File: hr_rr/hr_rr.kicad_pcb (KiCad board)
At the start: 2 copper layers, 32.2 x 20.5 mm, 44 parts, among them P1 Conn_01x02_Male, P2 Conn_01x02_Male, P3 Conn_01x02_Male, Q1 DMP21D5UFB4-7B, U1 TPS62746, U2 TPS63051_YFF, U3 NRF528XX-QFAA, U6 MCP73831, X1 Crystal_GND24, X2 32.768 kHz

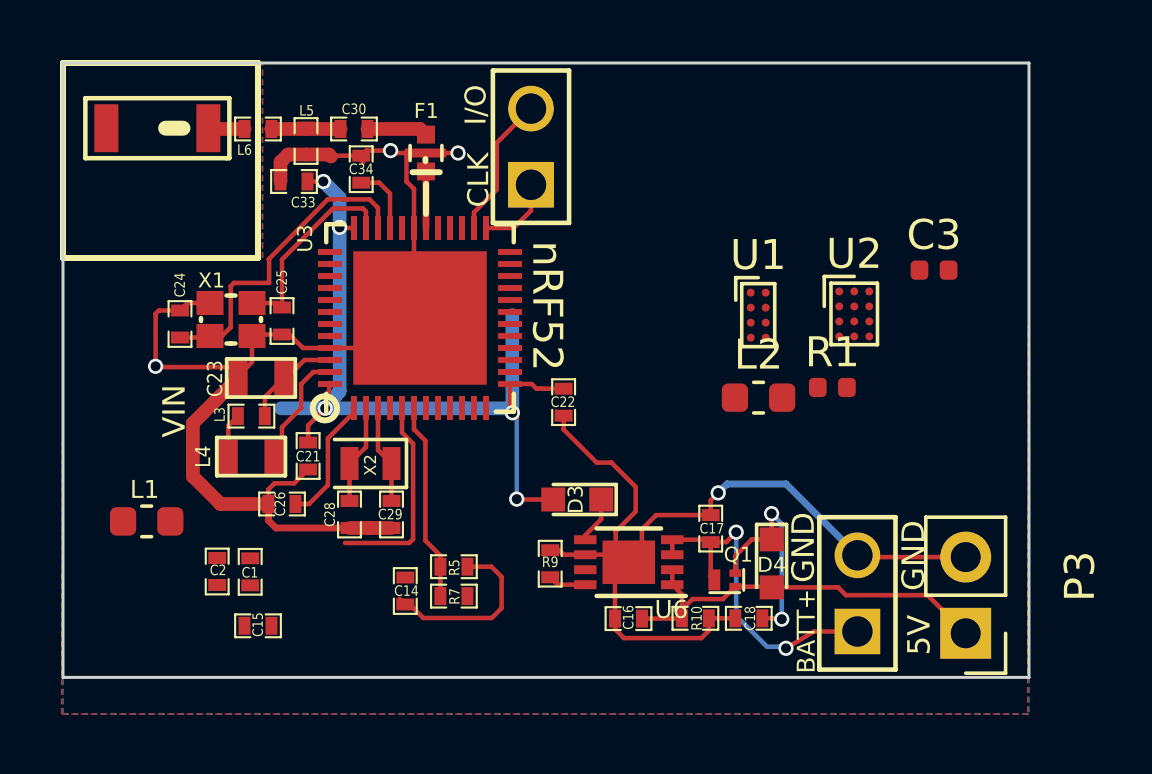
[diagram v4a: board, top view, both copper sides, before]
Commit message: Changed TPS63051 to VQFN Version, integrated power components.
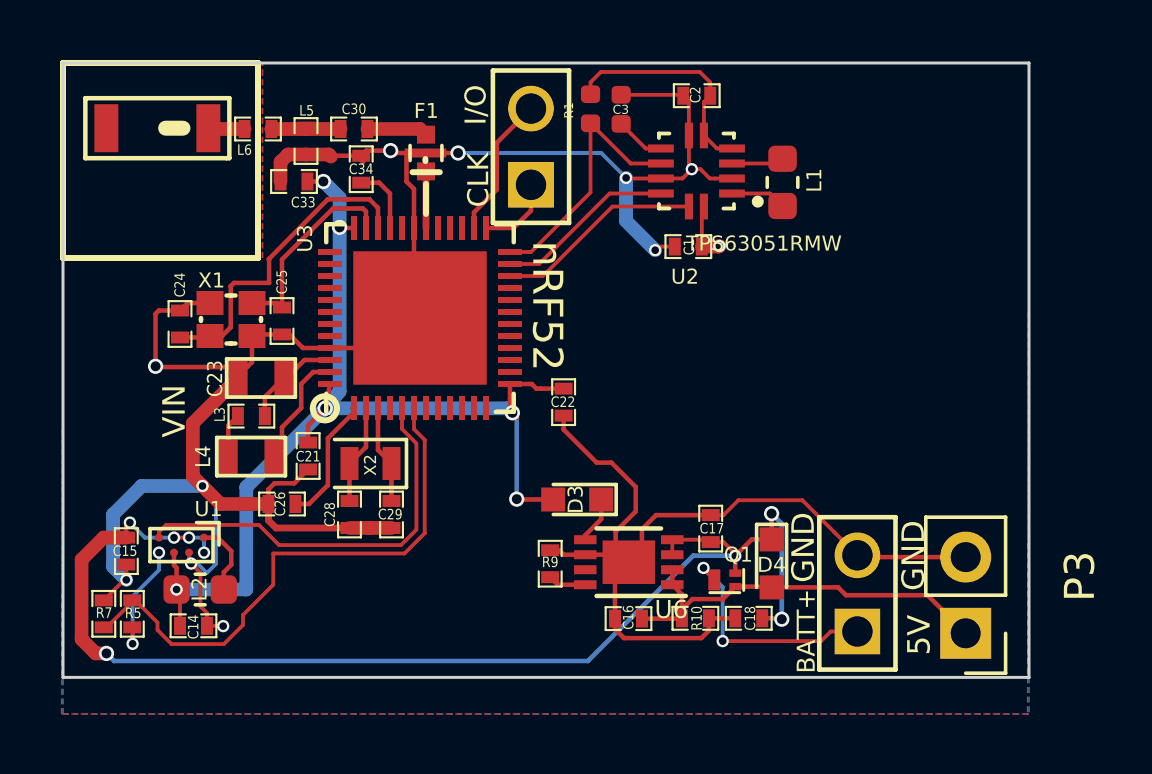
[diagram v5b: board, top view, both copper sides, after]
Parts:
- U2: value TPS63051_YFF -> TPS63051RMW; footprint Package_BGA:Texas_DSBGA-12_1.36x1.86mm_Layout3x4_P0.5mm -> footprints:QFN50P250X250X100-12N
- moved L1 24.0 mm to (289.9, 129.5), turned to 270 degrees
- moved C2 22.5 mm to (287.0, 126.6), turned to 180 degrees
- moved U1 20.7 mm to (269.9, 141.6), turned to 270 degrees
- moved L2 19.7 mm to (270.5, 143.1), turned to 180 degrees
- moved C1 18.2 mm to (286.7, 131.6), turned to 180 degrees
- moved R1 12.3 mm to (283.5, 127.0), turned to 270 degrees
- moved C3 11.7 mm to (284.5, 127.0), turned to 90 degrees
- moved R7 11.7 mm to (267.3, 143.9), turned to 270 degrees
- moved R5 10.8 mm to (268.2, 143.9), turned to 90 degrees
- moved C14 7.15 mm to (270.2, 144.3), turned to 0 degrees
- moved U2 7.10 mm to (287.0, 129.1), turned to 180 degrees
- moved C15 5.05 mm to (268.0, 141.8), turned to 270 degrees
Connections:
- C17 pad 1: /BATT_IN -> Vcc<BATT>
- U3 pad 22: Net-(U3-Pad22) -> /EN_TPS63051
- U3 pad 23: Net-(U3-Pad23) -> /ILIM0_TPS63051
- U3 pad 24: Net-(U3-Pad24) -> /PG_TPS63051
- U3 pad 7: /PG_TPS63051 -> Net-(U3-Pad7)
- U3 pad 8: /ILIM0_TPS63051 -> Net-(U3-Pad8)
- U3 pad 9: /ILIM1_TPS63051 -> Net-(U3-Pad9)
- U6 pad 3: /BATT_IN -> Vcc<BATT>
- U6 pad 4: /BATT_IN -> Vcc<BATT>
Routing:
- net Vcc<BATT>: track 7.20 -> 43.7 mm, vias 2 -> 9
- net DGND: track 85.0 -> 116.5 mm, vias 4 -> 10
- net /AIN_BAT_DIV_VOLTAGE: track 6.63 -> 18.5 mm
- net /BATT_IN: track 11.5 -> 0.00 mm, vias 2 -> 0
- net /PG_TPS63051: track 0.00 -> 8.96 mm
- net BATT_V: track 0.00 -> 8.05 mm, vias 0 -> 2
- net 3.3V_supply: track 0.00 -> 7.64 mm
- net 1.8V_supply: track 29.6 -> 36.9 mm, vias 5 -> 6
- net /EN_TPS63051: track 0.00 -> 6.92 mm
- net /LOAD_SW_CTRL: track 6.85 -> 13.6 mm
- net Net-(C14-Pad1): track 6.12 -> 0.00 mm
- net /ILIM0_TPS63051: track 0.00 -> 6.00 mm
- net Net-(R5-Pad1): track 0.00 -> 3.96 mm, vias 0 -> 2
- net Net-(L2-Pad1): track 0.00 -> 2.48 mm
- net Net-(L1-Pad2): track 0.00 -> 1.86 mm
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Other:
- net class Default: clearance 0.1524 -> 0.127; trace_width 0.4572 -> 0.127
- rule trace_clearance: 0.1524 -> 0.127
- rule via_min_drill: 0.3302 -> 0.254
- rule via_min_size: 0.152 -> 0.127

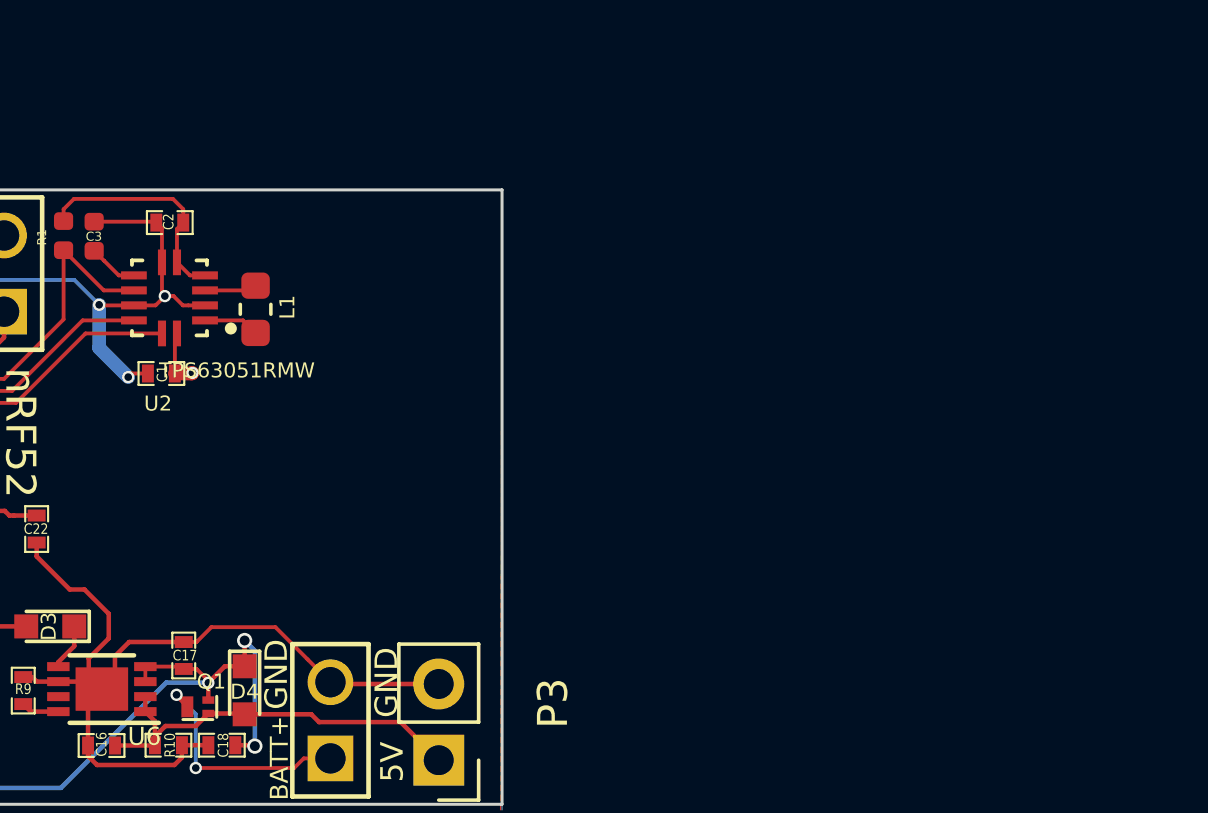
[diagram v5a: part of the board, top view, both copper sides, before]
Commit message: Added footprint for CMOS clock, added to PCB.
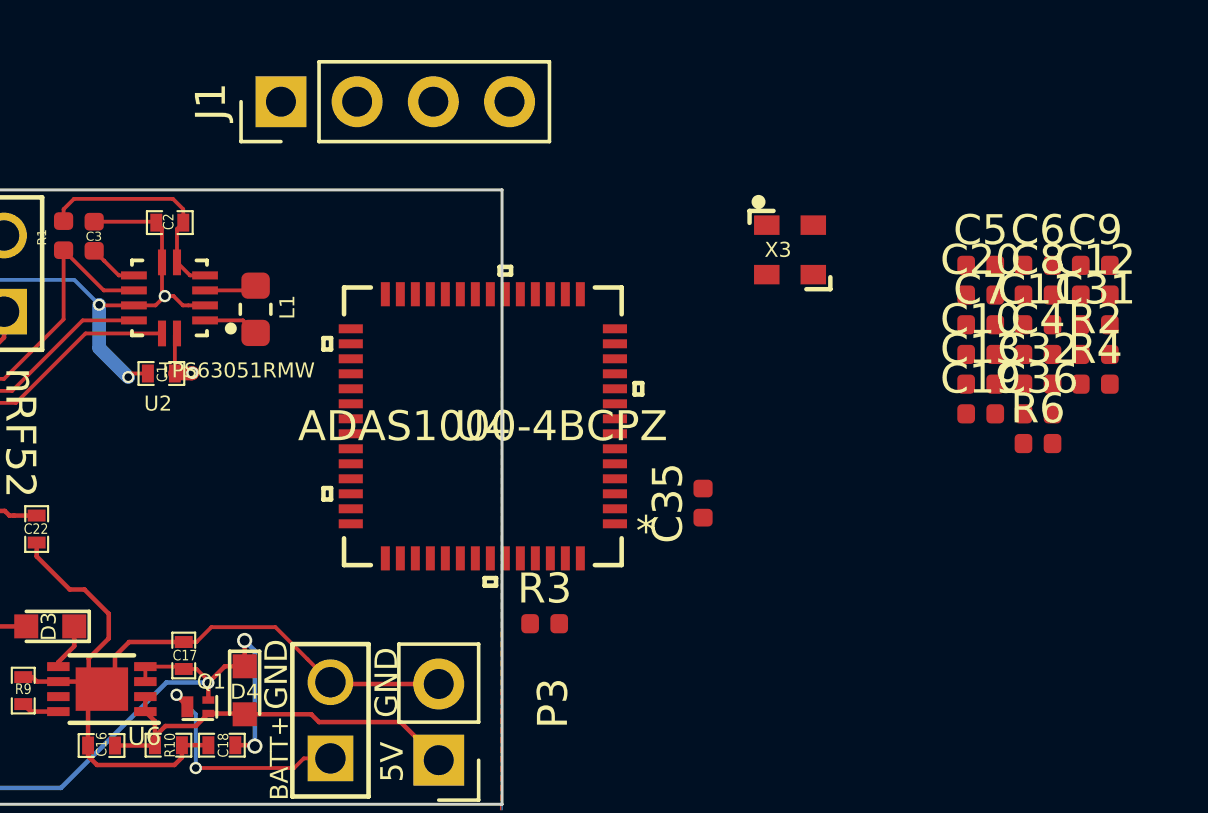
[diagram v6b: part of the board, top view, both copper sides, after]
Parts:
- added C10: 0.1uF, Capacitor_SMD:C_0402_1005Metric, F.Cu at (314.1, 131.0)
- added C11: 0.1uF, Capacitor_SMD:C_0402_1005Metric, F.Cu at (316.0, 130.0)
- added C12: 0.1uF, Capacitor_SMD:C_0402_1005Metric, F.Cu at (317.9, 129.0)
- added C13: 0.1uF, Capacitor_SMD:C_0402_1005Metric, F.Cu at (314.1, 132.0)
- added C19: 0.1uF, Capacitor_SMD:C_0402_1005Metric, F.Cu at (314.1, 133.0)
- added C20: 0.1uF, Capacitor_SMD:C_0402_1005Metric, F.Cu at (314.1, 129.0)
- added C31: 2.2 nF, Capacitor_SMD:C_0402_1005Metric, F.Cu at (317.9, 130.0)
- added C32: 0.1uF, Capacitor_SMD:C_0402_1005Metric, F.Cu at (316.0, 132.0)
- added C35: 10uF, Capacitor_SMD:C_0402_1005Metric, F.Cu at (304.8, 135.9)
- added C36: 15pF, Capacitor_SMD:C_0402_1005Metric, F.Cu at (316.0, 133.0)
- added C4: 4.7uF, Capacitor_SMD:C_0402_1005Metric, F.Cu at (316.0, 131.0)
- added C5: 4.7uF, Capacitor_SMD:C_0402_1005Metric, F.Cu at (314.1, 128.0)
- added C6: 0.1uF, Capacitor_SMD:C_0402_1005Metric, F.Cu at (316.0, 128.0)
- added C7: 0.1uF, Capacitor_SMD:C_0402_1005Metric, F.Cu at (314.1, 130.0)
- added C8: 0.1uF, Capacitor_SMD:C_0402_1005Metric, F.Cu at (316.0, 129.0)
- added C9: 0.1uF, Capacitor_SMD:C_0402_1005Metric, F.Cu at (317.9, 128.0)
- added J1: Electrodes, Connector_PinHeader_2.54mm:PinHeader_1x04_P2.54mm_Vertical, F.Cu at (290.7, 122.6)
- added R2: 4M, Resistor_SMD:R_0402_1005Metric, F.Cu at (317.9, 131.0)
- added R3: 40k, Resistor_SMD:R_0402_1005Metric, F.Cu at (299.5, 140.0)
- added R4: 100k, Resistor_SMD:R_0402_1005Metric, F.Cu at (317.9, 132.0)
- added R6: 30k, Resistor_SMD:R_0402_1005Metric, F.Cu at (316.0, 134.0)
- added U4: ADAS1000-4BCPZ, footprints:ADAS1000-4BCPZ, F.Cu at (297.5, 133.4)
- added X3: DSC1001, footprints:DSC1001DI5-008.1920T, F.Cu at (307.7, 127.5)
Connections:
- U3 pad 14: Net-(U3-Pad14) -> /~CS
- U3 pad 15: Net-(U3-Pad15) -> /~DRDY
- U3 pad 16: Net-(U3-Pad16) -> /SDI
- U3 pad 17: Net-(U3-Pad17) -> /SCLK
- U3 pad 18: Net-(U3-Pad18) -> /SDO
- U3 pad 19: Net-(U3-Pad19) -> /~PWDN
- U3 pad 20: Net-(U3-Pad20) -> /~RESET
- U3 pad 21: Net-(U3-Pad21) -> /CLK_DSC1001_STANDBY

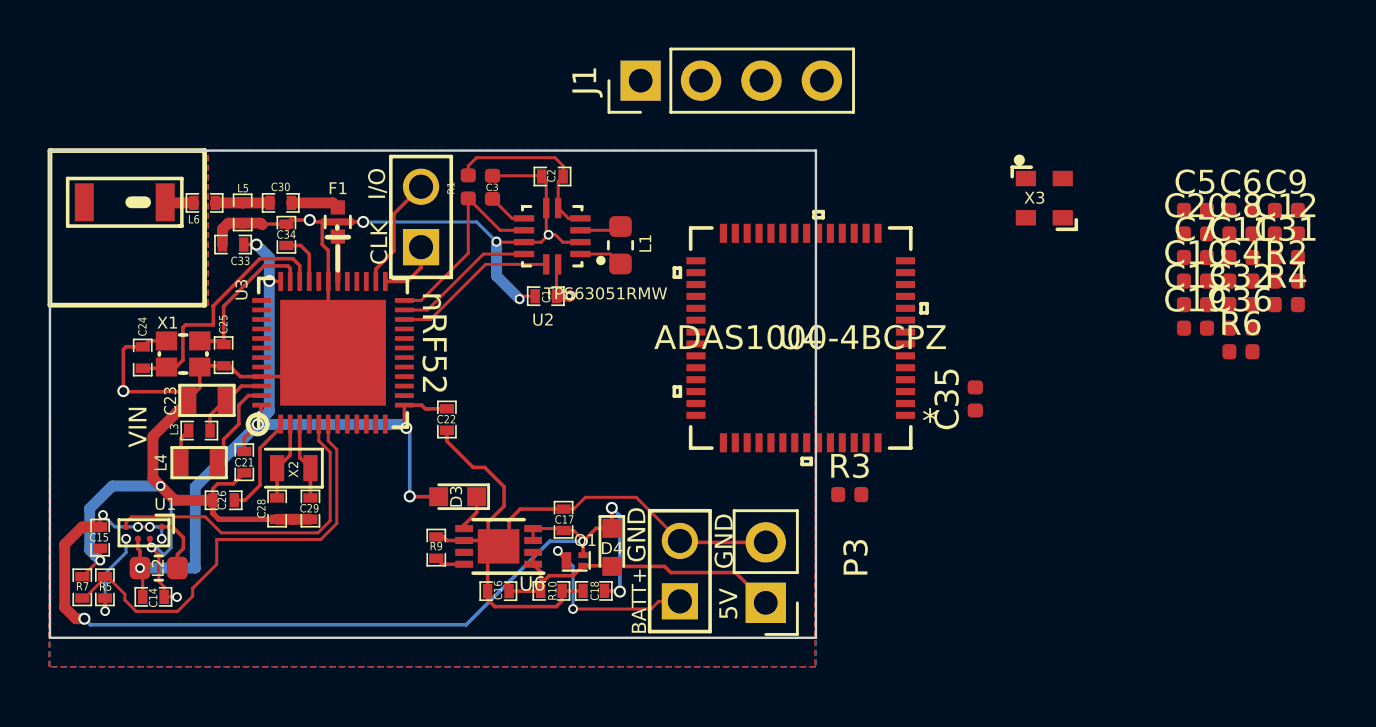
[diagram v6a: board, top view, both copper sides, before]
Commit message: Completed ADAS1000-4 portion, finalized PCB.
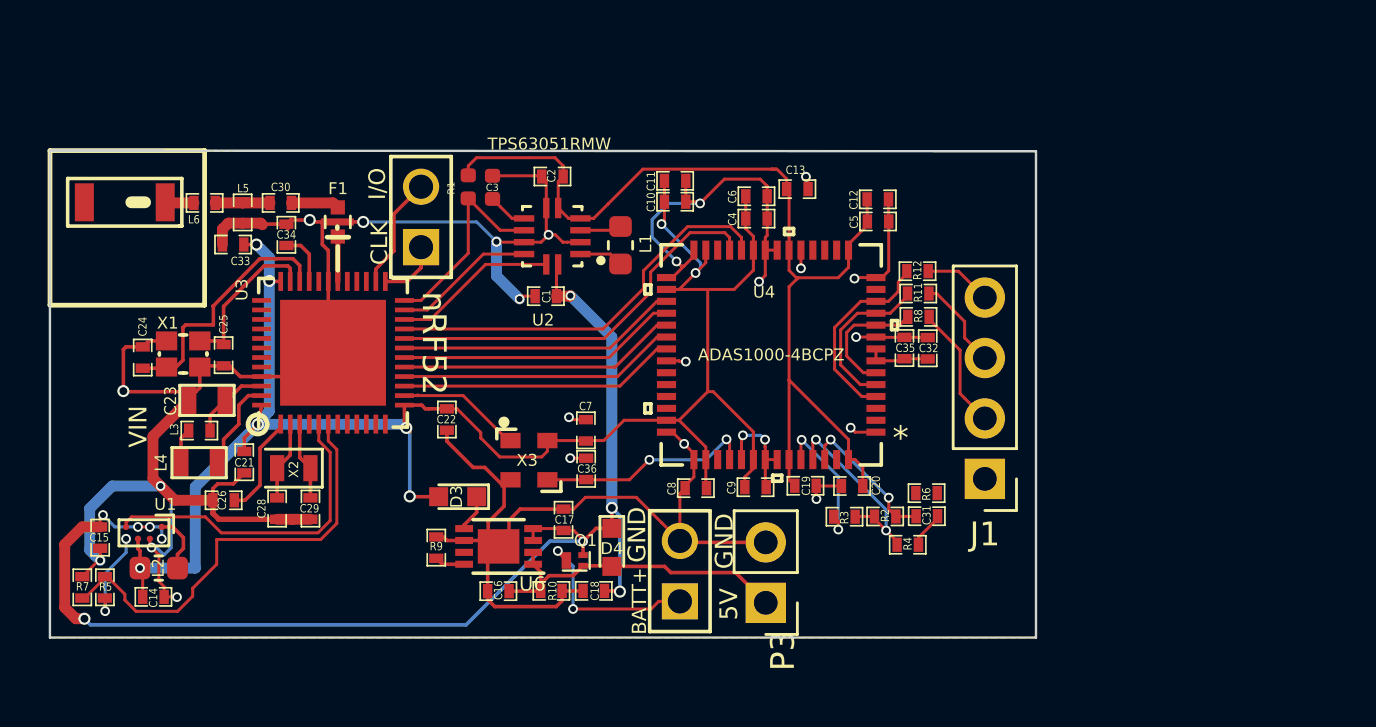
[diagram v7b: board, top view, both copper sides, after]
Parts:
- added R11: 30k, SM0402, F.Cu at (302.4, 131.5)
- added R12: 30k, SM0402, F.Cu at (302.4, 130.6)
- added R8: 30k, SM0402, F.Cu at (302.4, 132.5)
- C10, C11, C12, C13, C19, C20, C31, C32, C35, C36, C4, C5, C6, C7, C8, C9: footprint Capacitor_SMD:C_0402_1005Metric -> SM0402
- R2, R3, R4, R6: footprint Resistor_SMD:R_0402_1005Metric -> SM0402
- moved C36 28.2 mm to (288.4, 138.9), turned to 90 degrees
- moved C7 26.6 mm to (288.4, 137.3), turned to 270 degrees
- moved C8 25.3 mm to (293.1, 139.7)
- moved C9 25.2 mm to (295.6, 139.7), turned to 180 degrees
- moved X3 24.3 mm to (286.0, 138.5)
- moved C11 24.0 mm to (292.2, 126.8), turned to 180 degrees
- moved C10 22.1 mm to (292.2, 127.7), turned to 180 degrees
- moved J1 22.1 mm to (305.2, 139.3), turned to 180 degrees
- moved C4 20.5 mm to (295.6, 128.4), turned to 180 degrees
- moved C6 20.4 mm to (295.6, 127.4), turned to 180 degrees
- moved R2 19.6 mm to (301.0, 140.9), turned to 180 degrees
- moved R4 18.8 mm to (302.0, 142.1), turned to 180 degrees
- moved C31 18.6 mm to (302.8, 140.9), turned to 180 degrees
- moved C20 17.9 mm to (299.6, 139.6)
- moved C19 17.7 mm to (297.7, 139.6), turned to 180 degrees
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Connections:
- net Net-(C32-Pad1) renamed /VREF
- J1 pad 1: /e_LA -> /RLD_BIAS_ELECTRODE
- J1 pad 2: /e_LL -> /e_LA
- J1 pad 3: /e_RA -> /e_LL
- J1 pad 4: /RLD_BIAS_ELECTRODE -> /e_RA
- U3 pad 14: /~CS -> /CLK_DSC1001_STANDBY
- U3 pad 15: /~DRDY -> /~CS
- U3 pad 16: /SDI -> /~DRDY
- U3 pad 17: /SCLK -> /SDI
- U3 pad 18: /SDO -> /SCLK
- U3 pad 19: /~PWDN -> /SDO
- U3 pad 20: /~RESET -> /~PWDN
- U3 pad 21: /CLK_DSC1001_STANDBY -> /~RESET
- U4 pad 10: /e_LA -> Net-(R8-Pad2)
- U4 pad 11: /e_LL -> Net-(R11-Pad2)
- U4 pad 12: /e_RA -> Net-(R12-Pad2)
- U4 pad 4: /e_RA -> Net-(R12-Pad2)
- U4 pad 5: /e_LL -> Net-(R11-Pad2)
- U4 pad 6: /e_LA -> Net-(R8-Pad2)
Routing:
- net DGND: track 116.5 -> 156.6 mm, vias 10 -> 25
- net 1.8V_supply: track 36.9 -> 77.0 mm, vias 6 -> 8
- net 3.3V_supply: track 7.64 -> 42.3 mm
- net /~RESET: track 0.00 -> 17.1 mm
- net /~PWDN: track 0.00 -> 16.6 mm
- net /SDO: track 0.00 -> 11.8 mm
- net /SCLK: track 0.00 -> 11.8 mm
- net /SDI: track 0.00 -> 11.7 mm
- net /~DRDY: track 0.00 -> 11.7 mm
- net /~CS: track 0.00 -> 11.7 mm
- net Vcc<BATT>: track 43.7 -> 53.3 mm
- net /ADAS_XTAL2: track 0.00 -> 9.14 mm, vias 0 -> 2
- net Net-(R2-Pad2): track 0.00 -> 8.33 mm, vias 0 -> 2
- net Net-(R12-Pad2): track 0.00 -> 8.28 mm
- net Net-(R11-Pad2): track 0.00 -> 6.80 mm
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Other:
- board size 32.2 x 20.5 mm -> 41.5 x 20.5 mm

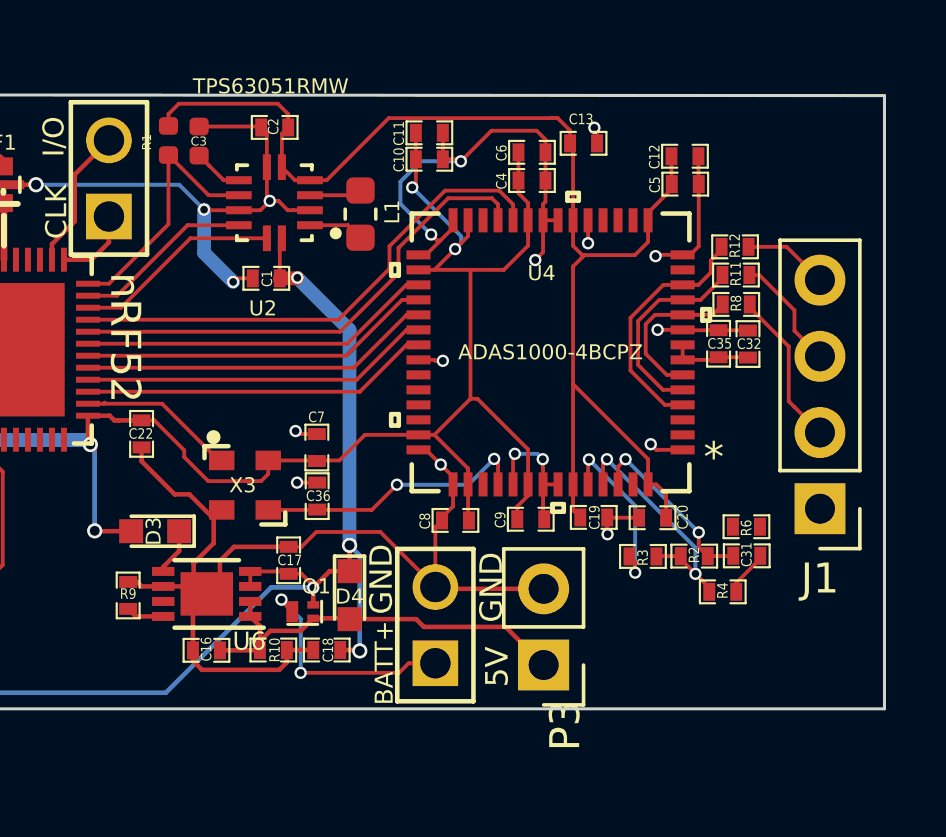
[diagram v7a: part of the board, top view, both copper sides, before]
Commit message: Added missing decoupling caps.
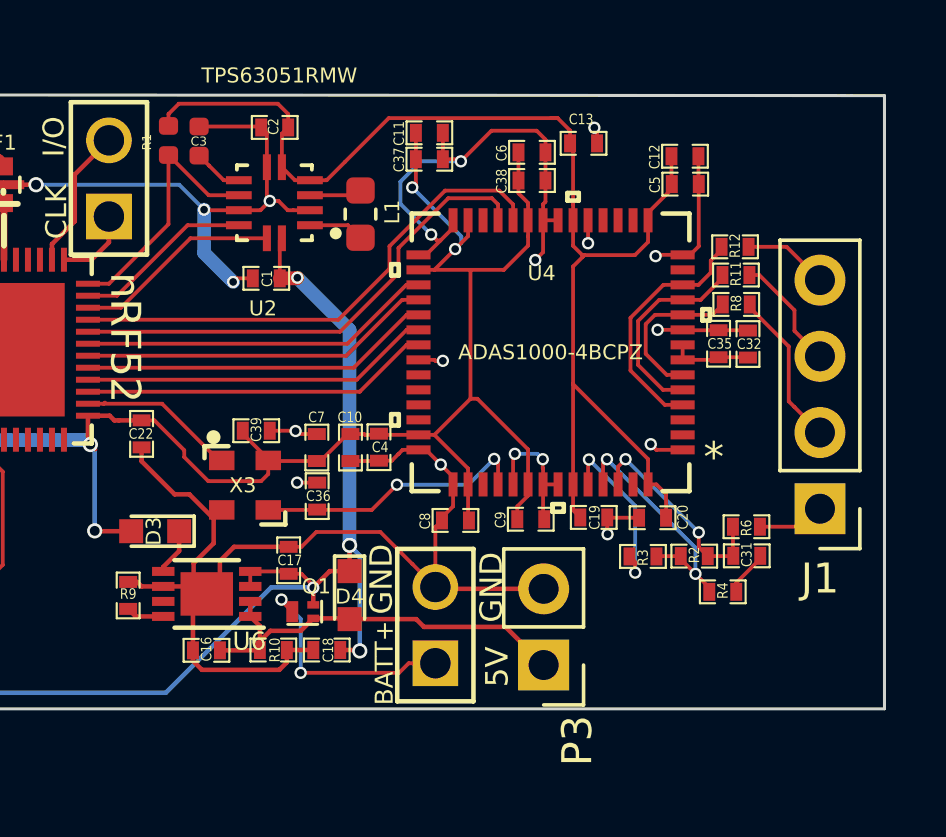
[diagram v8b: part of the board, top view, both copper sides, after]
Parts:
- added C10: 0.1uF, SM0402, F.Cu at (289.6, 137.3)
- added C39: 0.1uF, SM0402, F.Cu at (286.4, 136.7)
- added C4: 4.7uF, SM0402, F.Cu at (290.5, 137.2)
- C37: renamed from C10; value 0.1uF -> 2.2uF
- C38: renamed from C4; value 4.7uF -> 2.2uF
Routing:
- net DGND: track 156.6 -> 159.9 mm
- net /RLD_BIAS_ELECTRODE: track 0.00 -> 2.25 mm
- net 1.8V_supply: track 77.0 -> 78.4 mm
- net Net-(C31-Pad2): track 6.16 -> 7.14 mm
